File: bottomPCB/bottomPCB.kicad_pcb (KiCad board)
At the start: 2 copper layers, 10 parts, among them U1 ESP32-WROOM-32

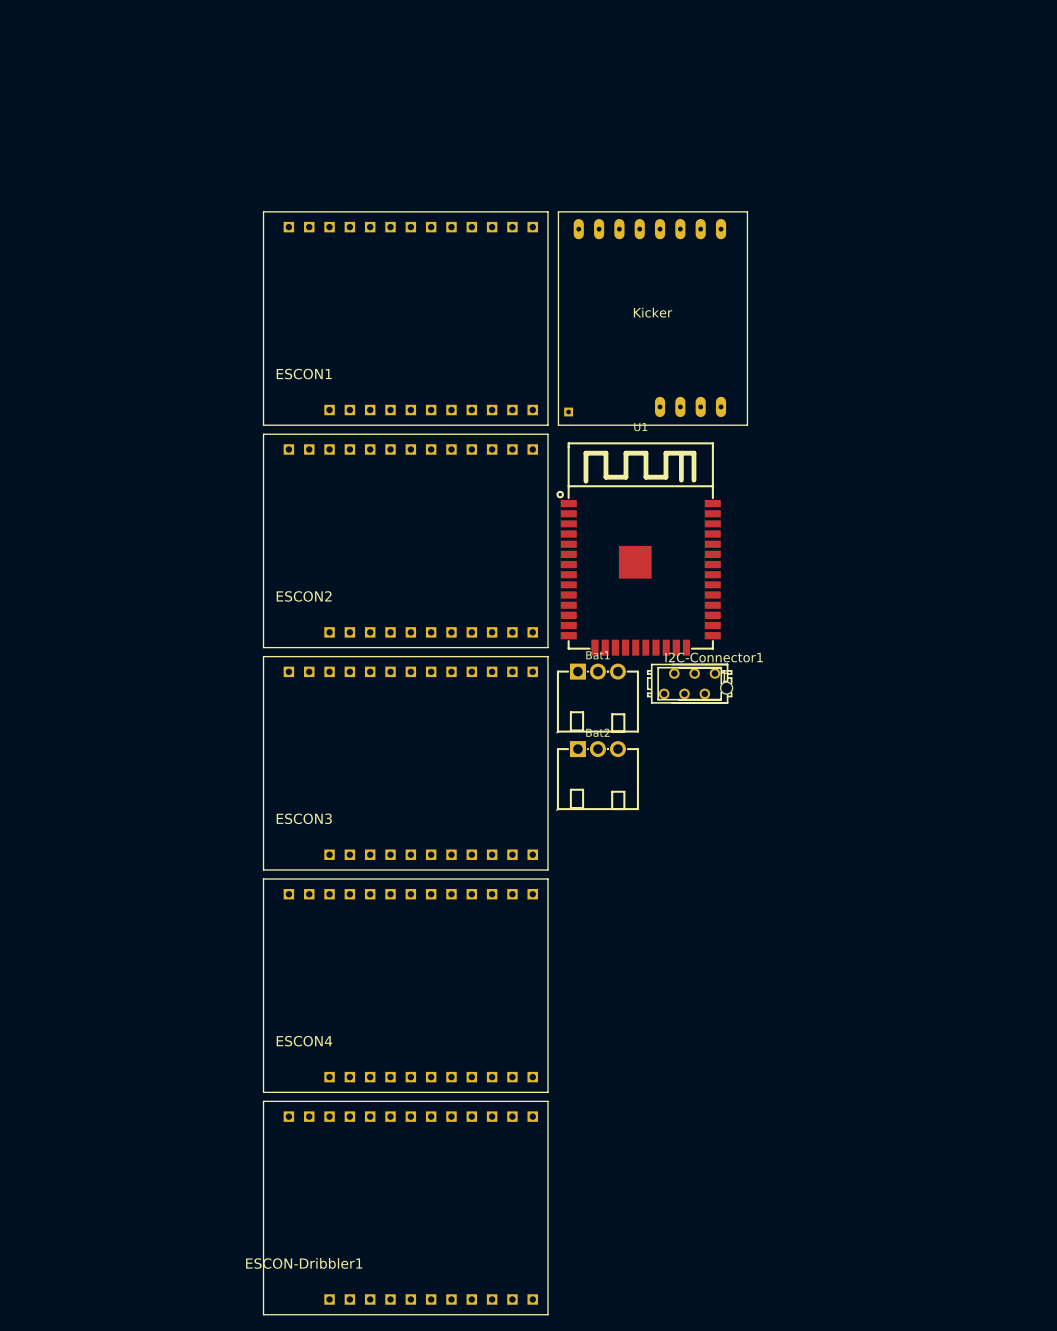
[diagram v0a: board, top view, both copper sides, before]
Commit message: added dribbler
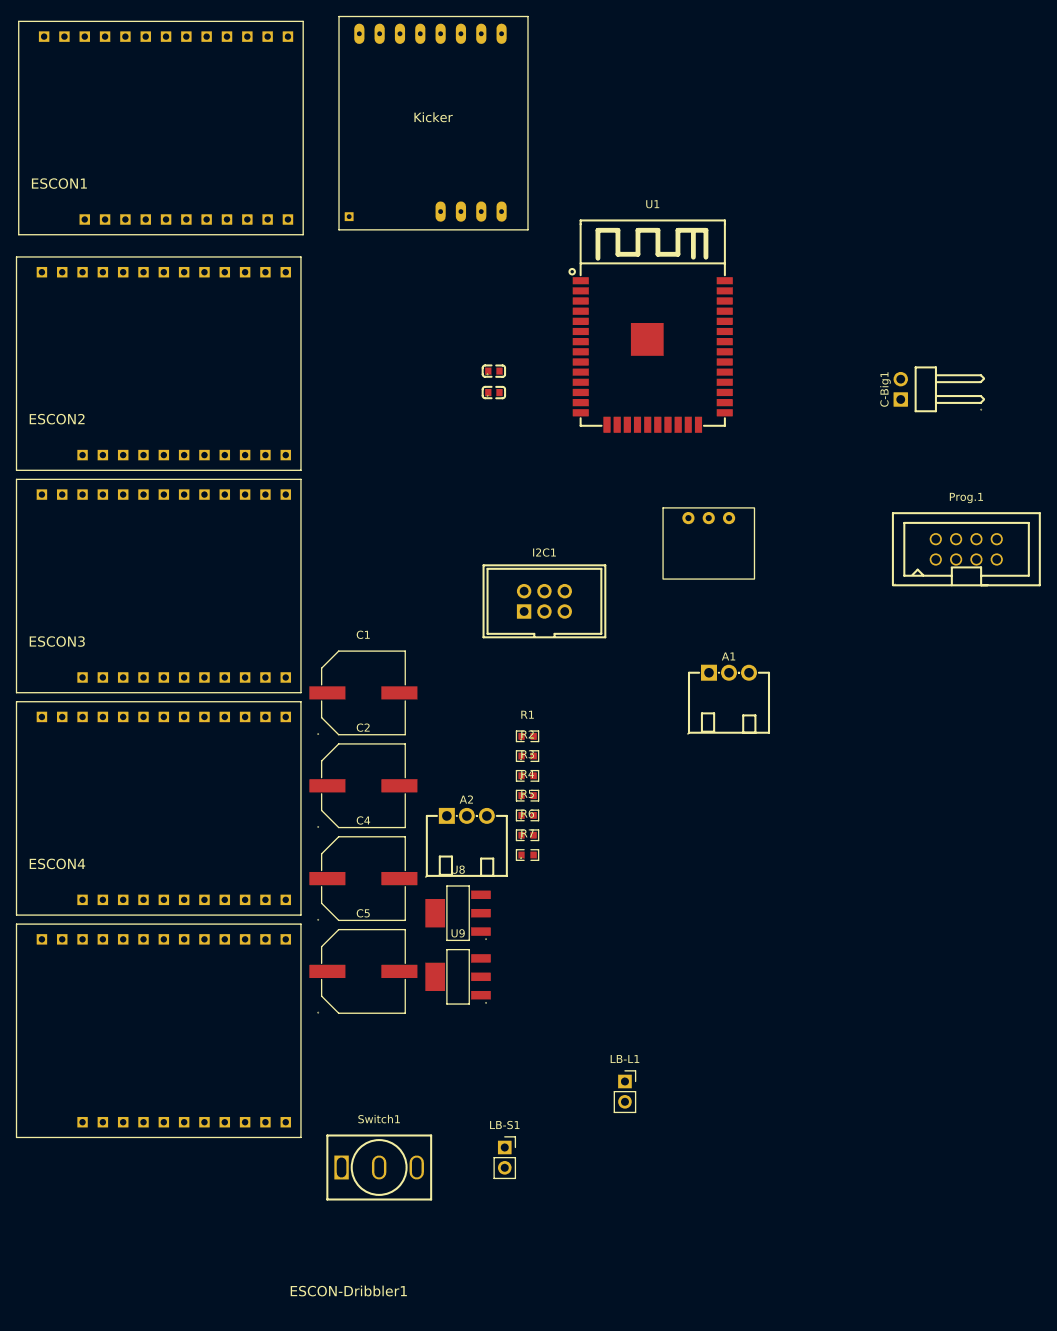
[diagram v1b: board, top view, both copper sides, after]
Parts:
- removed Bat1, Bat2: XH-3AW_C722865, BohleBots:CONN-TH_XH-3AW-C722865
- removed I2C-Connector1: MICROMATCH-6, BohleBots:MICROMATCH-6
- added A1: AKKU 1, BohleBots:CONN-TH_XH-3AW-C722865, F.Cu at (107.5, 94.7)
- added A2: AKKU 2, BohleBots:CONN-TH_XH-3AW-C722865, F.Cu at (74.8, 112.6)
- added C-Big1: Pinhead_1x02H, BohleBots:HDR-TH_2P-P2.54-H-M-W10.4, F.Cu at (129.0, 59.2)
- added C1: SMD-680uF, BohleBots:CAP-SMD_BD10.0-L10.3-W10.3-LS11.3-FD, F.Cu at (61.8, 97.2)
- added C2: RVT1A221M0605-C72494, BohleBots:CAP-SMD_BD10.0-L10.3-W10.3-LS11.3-FD, F.Cu at (61.8, 108.8)
- added C3: SMD-1uF, BohleBots:C0603, F.Cu at (78.1, 57.0)
- added C4: SMD-220uF, BohleBots:CAP-SMD_BD10.0-L10.3-W10.3-LS11.3-FD, F.Cu at (61.8, 120.4)
- added C5: SMD-220uF_50V, BohleBots:CAP-SMD_BD10.0-L10.3-W10.3-LS11.3-FD, F.Cu at (61.8, 132.0)
- added C6: SMD-100nF, BohleBots:C0603, F.Cu at (78.1, 59.6)
- added I2C1: Pfostenstecker_6_2x3, BohleBots:HDR-TH_6P-P2.54-V-F-R2-C3-S2.54-4, F.Cu at (84.5, 85.7)
- added LB-L1: Conn_01x02_Socket, Connector_PinSocket_2.54mm:PinSocket_1x02_P2.54mm_Vertical, F.Cu at (94.5, 145.8)
- added LB-S1: Conn_01x02_Socket, Connector_PinSocket_2.54mm:PinSocket_1x02_P2.54mm_Vertical, F.Cu at (79.5, 154.0)
- added Prog.1: Pfostenstecker_8_2x4, BohleBots:IDC-TH_8P-P2.54-V-R2-C4-S2.54, F.Cu at (137.2, 79.2)
- added R1: SMD-10k, BohleBots:R0603, F.Cu at (82.3, 102.6)
- added R2: SMD-10k, BohleBots:R0603, F.Cu at (82.3, 105.1)
- added R3: SMD-10k, BohleBots:R0603, F.Cu at (82.3, 107.5)
- added R4: SMD-10k, BohleBots:R0603, F.Cu at (82.3, 110.0)
- added R5: SMD-100R, BohleBots:R0603, F.Cu at (82.3, 112.5)
- added R6: SMD-10K, BohleBots:R0603, F.Cu at (82.3, 115.0)
- added R7: SMD-10K, BohleBots:R0603, F.Cu at (82.3, 117.4)
- added R78K2: ~, BohleBots:R785K, F.Cu at (105.0, 75.3)
- added Switch1: Switch, BohleBots:SW-TH_MT-0-103-A101-M200-RS, F.Cu at (63.8, 156.5)
- added U8: LM1117IMPX-3_3_NOPB, BohleBots:SOT-223_L6.5-W3.5-P2.30-LS7.0-BR, F.Cu at (73.7, 124.7)
- added U9: LM1117IMPX-3_3_NOPB, BohleBots:SOT-223_L6.5-W3.5-P2.30-LS7.0-BR, F.Cu at (73.7, 132.7)
- moved ESCON1 38.8 mm to (37.2, 27.8)
- moved ESCON-Dribbler1 38.0 mm to (36.9, 140.7)
- moved ESCON4 38.0 mm to (36.9, 112.9)
- moved ESCON2 38.0 mm to (36.9, 57.3)
- moved ESCON3 38.0 mm to (36.9, 85.1)
- moved Kicker1 36.7 mm to (58.8, 40.2)
- moved U1 27.9 mm to (98.0, 54.7)
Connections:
- ESCON-Dribbler1 pad P18: Net-(ESCON-Dribbler1-GND-PadP18) -> GND
- ESCON-Dribbler1 pad P4: unconnected-(ESCON-Dribbler1-VCC-PadP4) -> +16V
- ESCON-Dribbler1 pad P5: Net-(ESCON-Dribbler1-GND-PadP18) -> GND
- ESCON1 pad P1: unconnected-(ESCON1-M1-PadP1) -> Net-(EC 20 flat1-M1)
- ESCON1 pad P15: unconnected-(ESCON1-D3-PadP15) -> DIR1
- ESCON1 pad P16: unconnected-(ESCON1-D2-PadP16) -> ENA
- ESCON1 pad P17: unconnected-(ESCON1-D1-PadP17) -> PWM1
- ESCON1 pad P18: Net-(ESCON1-GND-PadP18) -> GND
- ESCON1 pad P2: unconnected-(ESCON1-M2-PadP2) -> Net-(EC 20 flat1-M2)
- ESCON1 pad P3: unconnected-(ESCON1-M3-PadP3) -> Net-(EC 20 flat1-M3)
- ESCON1 pad P4: unconnected-(ESCON1-VCC-PadP4) -> +16V
- ESCON1 pad P5: Net-(ESCON1-GND-PadP18) -> GND
- ESCON1 pad P6: unconnected-(ESCON1-+5V-PadP6) -> Net-(EC 20 flat1-VCC)
- ESCON1 pad P7: unconnected-(ESCON1-H1-PadP7) -> Net-(EC 20 flat1-Hall_1)
- ESCON1 pad P8: unconnected-(ESCON1-H2-PadP8) -> Net-(EC 20 flat1-Hall_2)
- ESCON1 pad P9: unconnected-(ESCON1-H3-PadP9) -> Net-(EC 20 flat1-Hall_3)
- ESCON2 pad P1: unconnected-(ESCON2-M1-PadP1) -> Net-(EC 20 flat2-M1)
- ESCON2 pad P15: unconnected-(ESCON2-D3-PadP15) -> DIR2
- ESCON2 pad P16: unconnected-(ESCON2-D2-PadP16) -> ENA
- ESCON2 pad P17: unconnected-(ESCON2-D1-PadP17) -> PWM2
- ESCON2 pad P18: Net-(ESCON2-GND-PadP18) -> GND
- ESCON2 pad P2: unconnected-(ESCON2-M2-PadP2) -> Net-(EC 20 flat2-M2)
- ESCON2 pad P3: unconnected-(ESCON2-M3-PadP3) -> Net-(EC 20 flat2-M3)
- ESCON2 pad P4: unconnected-(ESCON2-VCC-PadP4) -> +16V
- ESCON2 pad P5: Net-(ESCON2-GND-PadP18) -> GND
- ESCON2 pad P6: unconnected-(ESCON2-+5V-PadP6) -> Net-(EC 20 flat2-VCC)
- ESCON2 pad P7: unconnected-(ESCON2-H1-PadP7) -> Net-(EC 20 flat2-Hall_1)
- ESCON2 pad P8: unconnected-(ESCON2-H2-PadP8) -> Net-(EC 20 flat2-Hall_2)
- ESCON2 pad P9: unconnected-(ESCON2-H3-PadP9) -> Net-(EC 20 flat2-Hall_3)
- ESCON3 pad P1: unconnected-(ESCON3-M1-PadP1) -> Net-(EC 20 flat3-M1)
- ESCON3 pad P15: unconnected-(ESCON3-D3-PadP15) -> DIR3
- ESCON3 pad P16: unconnected-(ESCON3-D2-PadP16) -> ENA
- ESCON3 pad P17: unconnected-(ESCON3-D1-PadP17) -> PWM3
- ESCON3 pad P18: Net-(ESCON3-GND-PadP18) -> GND
- ESCON3 pad P2: unconnected-(ESCON3-M2-PadP2) -> Net-(EC 20 flat3-M2)
- ESCON3 pad P3: unconnected-(ESCON3-M3-PadP3) -> Net-(EC 20 flat3-M3)
- ESCON3 pad P4: unconnected-(ESCON3-VCC-PadP4) -> +16V
- ESCON3 pad P5: Net-(ESCON3-GND-PadP18) -> GND
- ESCON3 pad P6: unconnected-(ESCON3-+5V-PadP6) -> Net-(EC 20 flat3-VCC)
- ESCON3 pad P7: unconnected-(ESCON3-H1-PadP7) -> Net-(EC 20 flat3-Hall_1)
- ESCON3 pad P8: unconnected-(ESCON3-H2-PadP8) -> Net-(EC 20 flat3-Hall_2)
- ESCON3 pad P9: unconnected-(ESCON3-H3-PadP9) -> Net-(EC 20 flat3-Hall_3)
- ESCON4 pad P1: unconnected-(ESCON4-M1-PadP1) -> Net-(EC 20 flat4-M1)
- ESCON4 pad P15: unconnected-(ESCON4-D3-PadP15) -> DIR4
- ESCON4 pad P16: unconnected-(ESCON4-D2-PadP16) -> ENA
- ESCON4 pad P17: unconnected-(ESCON4-D1-PadP17) -> PWM4
- ESCON4 pad P18: Net-(ESCON4-GND-PadP18) -> GND
- ESCON4 pad P2: unconnected-(ESCON4-M2-PadP2) -> Net-(EC 20 flat4-M2)
- ESCON4 pad P3: unconnected-(ESCON4-M3-PadP3) -> Net-(EC 20 flat4-M3)
- ESCON4 pad P4: unconnected-(ESCON4-VCC-PadP4) -> +16V
- ESCON4 pad P5: Net-(ESCON4-GND-PadP18) -> GND
- ESCON4 pad P6: unconnected-(ESCON4-+5V-PadP6) -> Net-(EC 20 flat4-VCC)
- ESCON4 pad P7: unconnected-(ESCON4-H1-PadP7) -> Net-(EC 20 flat4-Hall_1)
- ESCON4 pad P8: unconnected-(ESCON4-H2-PadP8) -> Net-(EC 20 flat4-Hall_2)
- ESCON4 pad P9: unconnected-(ESCON4-H3-PadP9) -> Net-(EC 20 flat4-Hall_3)
- Kicker1 pad GND1: Net-(Kicker1-GND-PadGND1) -> GND
- Kicker1 pad GND2: Net-(Kicker1-GND-PadGND1) -> GND
- Kicker1 pad GND3: Net-(Kicker1-GND-PadGND1) -> GND
- Kicker1 pad GND4: Net-(Kicker1-GND-PadGND1) -> GND
- Kicker1 pad GND5: Net-(Kicker1-GND-PadGND1) -> GND
- Kicker1 pad GND6: Net-(Kicker1-GND-PadGND1) -> GND
- Kicker1 pad GND7: Net-(Kicker1-GND-PadGND1) -> GND
- Kicker1 pad GND8: Net-(Kicker1-GND-PadGND1) -> GND
- Kicker1 pad SIG: unconnected-(Kicker1-PadSIG) -> KICK
- Kicker1 pad V+1: Net-(Kicker1-V+-PadV+1) -> +16V
- Kicker1 pad V+2: Net-(Kicker1-V+-PadV+1) -> +16V
- Kicker1 pad V+3: Net-(Kicker1-V+-PadV+1) -> +16V
- U1 pad 1: unconnected-(U1-GND-Pad1) -> GND
- U1 pad 10: unconnected-(U1-IO25-Pad10) -> PWM3
- U1 pad 11: unconnected-(U1-IO26-Pad11) -> PWM4
- U1 pad 12: unconnected-(U1-IO27-Pad12) -> PWM5
- U1 pad 13: unconnected-(U1-IO14-Pad13) -> DIR1
- U1 pad 14: unconnected-(U1-IO12-Pad14) -> DIR2
- U1 pad 15: unconnected-(U1-GND-Pad15) -> GND
- U1 pad 16: unconnected-(U1-IO13-Pad16) -> DIR3
- U1 pad 24: unconnected-(U1-IO2-Pad24) -> KICK
- U1 pad 25: unconnected-(U1-IO0-Pad25) -> BOOT
- U1 pad 26: unconnected-(U1-IO4-Pad26) -> ENA
- U1 pad 3: unconnected-(U1-EN-Pad3) -> EN
- U1 pad 33: unconnected-(U1-IO21-Pad33) -> SDA
- U1 pad 34: unconnected-(U1-RXD0-Pad34) -> RX
- U1 pad 35: unconnected-(U1-TXD0-Pad35) -> TX
- U1 pad 36: unconnected-(U1-IO22-Pad36) -> SCL
- U1 pad 37: unconnected-(U1-IO23-Pad37) -> DIR4
- U1 pad 38: unconnected-(U1-GND-Pad38) -> GND
- U1 pad 39: unconnected-(U1-GND-Pad39) -> GND
- U1 pad 6: unconnected-(U1-IO34-Pad6) -> BARRIER
- U1 pad 8: unconnected-(U1-IO32-Pad8) -> PWM1
- U1 pad 9: unconnected-(U1-IO33-Pad9) -> PWM2

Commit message: Import to PCB editor
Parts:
- removed C1: SMD-680uF, BohleBots:CAP-SMD_BD10.0-L10.3-W10.3-LS11.3-FD
- removed C2: RVT1A221M0605-C72494, BohleBots:CAP-SMD_BD10.0-L10.3-W10.3-LS11.3-FD
- removed ESCON-Dribbler1: 24_2, BohleBots:ESCOM_24_2
- removed R78K2: ~, BohleBots:R785K
- removed Switch1: Switch, BohleBots:SW-TH_MT-0-103-A101-M200-RS
- added C7: RVT1A221M0605-C72494, BohleBots:CAP-SMD_BD10.0-L10.3-W10.3-LS11.3-FD, F.Cu at (245.1, 46.3)
- added C8: SMD-680uF, BohleBots:CAP-SMD_BD10.0-L10.3-W10.3-LS11.3-FD, F.Cu at (245.1, 57.9)
- added D36V28FX1: 5V, BohleBots:D36V28FX, F.Cu at (248.7, 87.9)
- added J1: Conn_01x03, Connector_PinSocket_2.54mm:PinSocket_1x03_P2.54mm_Vertical, F.Cu at (254.7, 52.5)
- added J2: Conn_02x03_Odd_Even, Connector_PinSocket_2.54mm:PinSocket_2x03_P2.54mm_Vertical, F.Cu at (261.8, 52.5)
- added J3: Conn_01x02, Connector_PinSocket_2.54mm:PinSocket_1x02_P2.54mm_Vertical, F.Cu at (259.3, 62.2)
- added J4: Conn_02x03_Odd_Even, Connector_PinSocket_2.54mm:PinSocket_2x03_P2.54mm_Vertical, F.Cu at (269.0, 52.5)
- added J5: 1-84953-1, 1-84953-1:1849531, F.Cu at (226.9, 24.8)
- added J6: 1-84953-1, 1-84953-1:1849531, F.Cu at (226.9, 38.1)
- added J7: 1-84953-1, 1-84953-1:1849531, F.Cu at (226.9, 51.3)
- added J8: 1-84953-1, 1-84953-1:1849531, F.Cu at (226.9, 64.6)
- added LED1: led1, BohleBots:LED-SMD_6P-L5.0-W5.0-TL_TC5050RGBF08, F.Cu at (268.5, 20.4)
- added R10: SMD-220R, BohleBots:R0603, F.Cu at (258.2, 28.4)
- added R11: SMD-10k, BohleBots:R0603, F.Cu at (262.2, 18.5)
- added R12: SMD-10k, BohleBots:R0603, F.Cu at (262.2, 21.0)
- added R13: SMD-10k, BohleBots:R0603, F.Cu at (262.2, 23.5)
- added R8: SMD-220R, BohleBots:R0603, F.Cu at (258.2, 23.5)
- added R9: SMD-220R, BohleBots:R0603, F.Cu at (258.2, 25.9)
- added Taster_LED1: ~, BohleBots:TASTER_LED, F.Cu at (256.3, 100.3)
- added U2: XT30_horizontal, BohleBots:CONN-TH_XT30PW-M, F.Cu at (257.9, 117.9)
- moved LB-S1 210.1 mm to (268.5, 62.2)
- moved C4 207.5 mm to (245.1, 23.1)
- moved C5 207.5 mm to (245.1, 34.7)
- moved R6 200.6 mm to (258.2, 18.5)
- moved R7 200.6 mm to (258.2, 21.0)
- moved A2 195.1 mm to (267.4, 81.5)
- moved R1 191.4 mm to (254.3, 18.5)
- moved R2 191.4 mm to (254.3, 21.0)
- moved R3 191.4 mm to (254.3, 23.5)
- moved R4 191.4 mm to (254.3, 25.9)
- moved R5 191.4 mm to (254.3, 28.4)
- moved C3 190.7 mm to (266.1, 24.9)
- moved C6 190.7 mm to (266.1, 27.6)
- moved LB-L1 188.8 mm to (263.9, 62.2)
- moved I2C1 180.8 mm to (260.6, 45.0)
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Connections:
- C-Big1 pad 1: +16V -> +BATT
- C5 pad 1: +16V -> +BATT
- C6 pad 2: +16V -> +BATT
- ESCON1 pad P4: +16V -> +BATT
- ESCON2 pad P4: +16V -> +BATT
- ESCON3 pad P4: +16V -> +BATT
- ESCON4 pad P4: +16V -> +BATT
- I2C1 pad 6: unconnected-(I2C1-Pad6) -> P23
- Kicker1 pad V+1: +16V -> +BATT
- Kicker1 pad V+2: +16V -> +BATT
- Kicker1 pad V+3: +16V -> +BATT
- U1 pad 13: DIR1 -> LED_G
- U1 pad 14: DIR2 -> GPIO12
- U1 pad 16: DIR3 -> GPIO13
- U1 pad 2: unconnected-(U1-3V3-Pad2) -> +3.3V
- U1 pad 23: unconnected-(U1-IO15-Pad23) -> LED_B
- U1 pad 24: KICK -> ENA
- U1 pad 26: ENA -> KICK
- U1 pad 27: unconnected-(U1-IO16-Pad27) -> DIR1
- U1 pad 28: unconnected-(U1-IO17-Pad28) -> DIR2
- U1 pad 29: unconnected-(U1-IO5-Pad29) -> LED_R
- U1 pad 30: unconnected-(U1-IO18-Pad30) -> DIR3
- U1 pad 31: unconnected-(U1-IO19-Pad31) -> DIR4
- U1 pad 37: DIR4 -> P23
- U1 pad 4: unconnected-(U1-SENSOR_VP-Pad4) -> IN_36
- U1 pad 5: unconnected-(U1-SENSOR_VN-Pad5) -> BARRIER
- U1 pad 6: BARRIER -> IN_34
- U1 pad 7: unconnected-(U1-IO35-Pad7) -> IN_35

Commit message: first placement of electronics on pcb
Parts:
- moved A1 348.2 mm to (-78.8, 35.0), turned to 90 degrees
- moved C-Big1 346.5 mm to (-49.4, -25.6), turned to 45 degrees
- moved Kicker1 319.0 mm to (-80.9, -16.5), turned to -90 degrees
- moved C3 310.4 mm to (-33.3, 106.5)
- moved R6 297.6 mm to (-25.2, 109.0)
- moved LED1 291.2 mm to (-14.9, 87.3), turned to -20 degrees
- moved R7 289.6 mm to (-17.5, 109.5)
- moved Prog.1 286.2 mm to (-17.4, 96.2), turned to -20 degrees
- moved J3 274.4 mm to (-15.0, 72.2)
- moved J7 273.9 mm to (-45.0, 17.8), turned to -90 degrees
- moved R10 273.1 mm to (-7.75, 90.5)
- moved R8 273.1 mm to (-7.75, 85.5)
- moved R9 273.1 mm to (-7.75, 88.0)
- moved J8 253.3 mm to (-12.0, -19.7), turned to -90 degrees
- moved Taster_LED1 246.3 mm to (10.1, 96.1)
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
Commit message: draft of pcb outline + placement of electronics
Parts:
- J1: value Conn_01x03 -> Conn_01x03_Pin
- moved R11 333.3 mm to (-17.4, -11.3), turned to 90 degrees
- moved R12 331.4 mm to (-15.0, -11.3), turned to 90 degrees
- moved R13 329.4 mm to (-12.5, -11.3), turned to 90 degrees
- moved J2 327.6 mm to (-24.5, -2.83)
- moved LB-S1 314.8 mm to (-27.0, -7.28), turned to 90 degrees
- moved R4 309.8 mm to (-20.0, -11.3), turned to -90 degrees
- moved C5 301.6 mm to (-73.0, -10.0)
- moved C8 300.4 mm to (-73.0, 1.00)
- moved LB-L1 292.5 mm to (17.1, 76.9), turned to 135 degrees
- moved C6 290.8 mm to (-69.0, 24.0), turned to 90 degrees
- moved R5 283.7 mm to (18.0, 84.7), turned to 90 degrees
- moved C4 239.9 mm to (25.5, 64.6), turned to 180 degrees
- moved U8 232.4 mm to (22.5, 49.0), turned to 90 degrees
- moved J4 231.2 mm to (38.1, 40.5), turned to -90 degrees
- moved U9 227.2 mm to (30.5, 49.0), turned to 90 degrees
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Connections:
- J1 pad 1: PWM5 -> GND
- J1 pad 3: GND -> PWM5
- J2 pad 1: IN_34 -> IN_39
- J2 pad 3: IN_35 -> IN_34
- J2 pad 5: IN_36 -> IN_35
- U1 pad 11: PWM4 -> PWM2
- U1 pad 27: DIR1 -> DIR2
- U1 pad 28: DIR2 -> DIR1
- U1 pad 30: DIR3 -> PWM1
- U1 pad 4: IN_36 -> BARRIER
- U1 pad 5: BARRIER -> IN_39
- U1 pad 8: PWM1 -> PWM4
- U1 pad 9: PWM2 -> DIR3
